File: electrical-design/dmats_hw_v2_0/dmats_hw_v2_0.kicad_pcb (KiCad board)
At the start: 2 copper layers, 2 parts, among them J1 Conn_01x05, U1 ABX00042

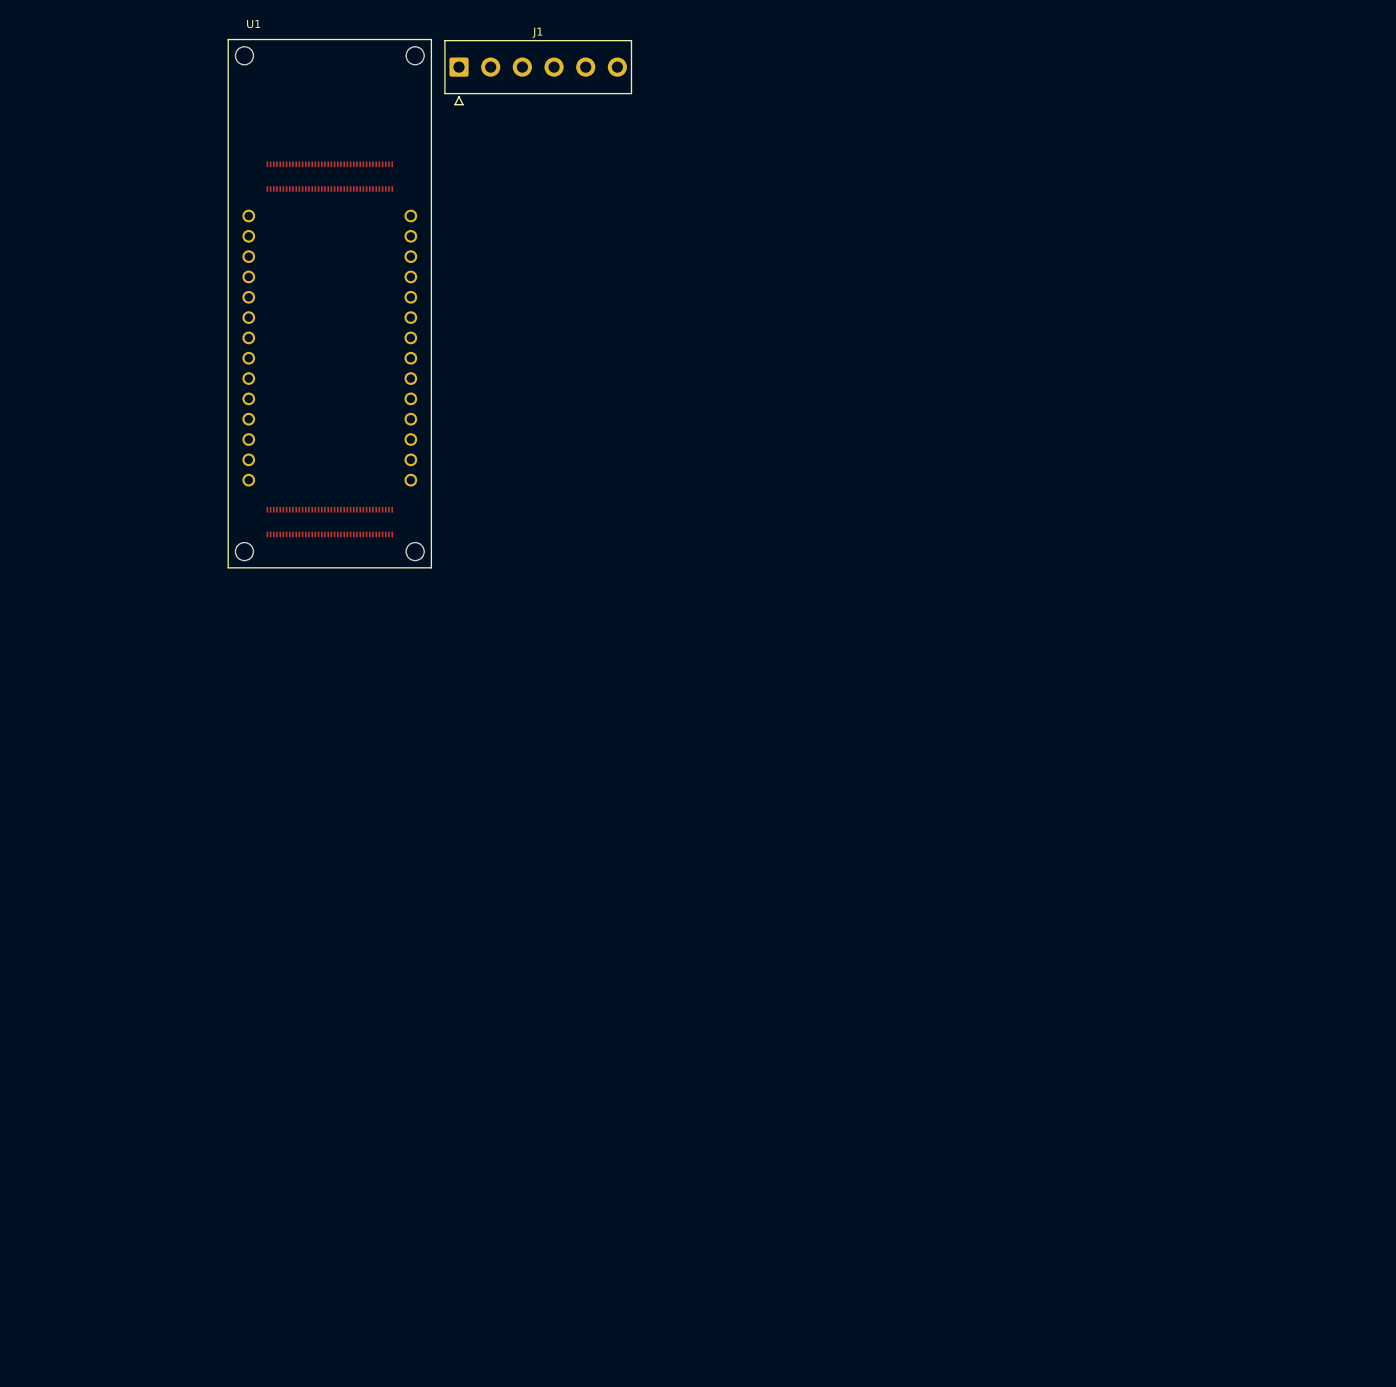
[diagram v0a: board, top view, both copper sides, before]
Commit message: bulk of PCB design layout complete
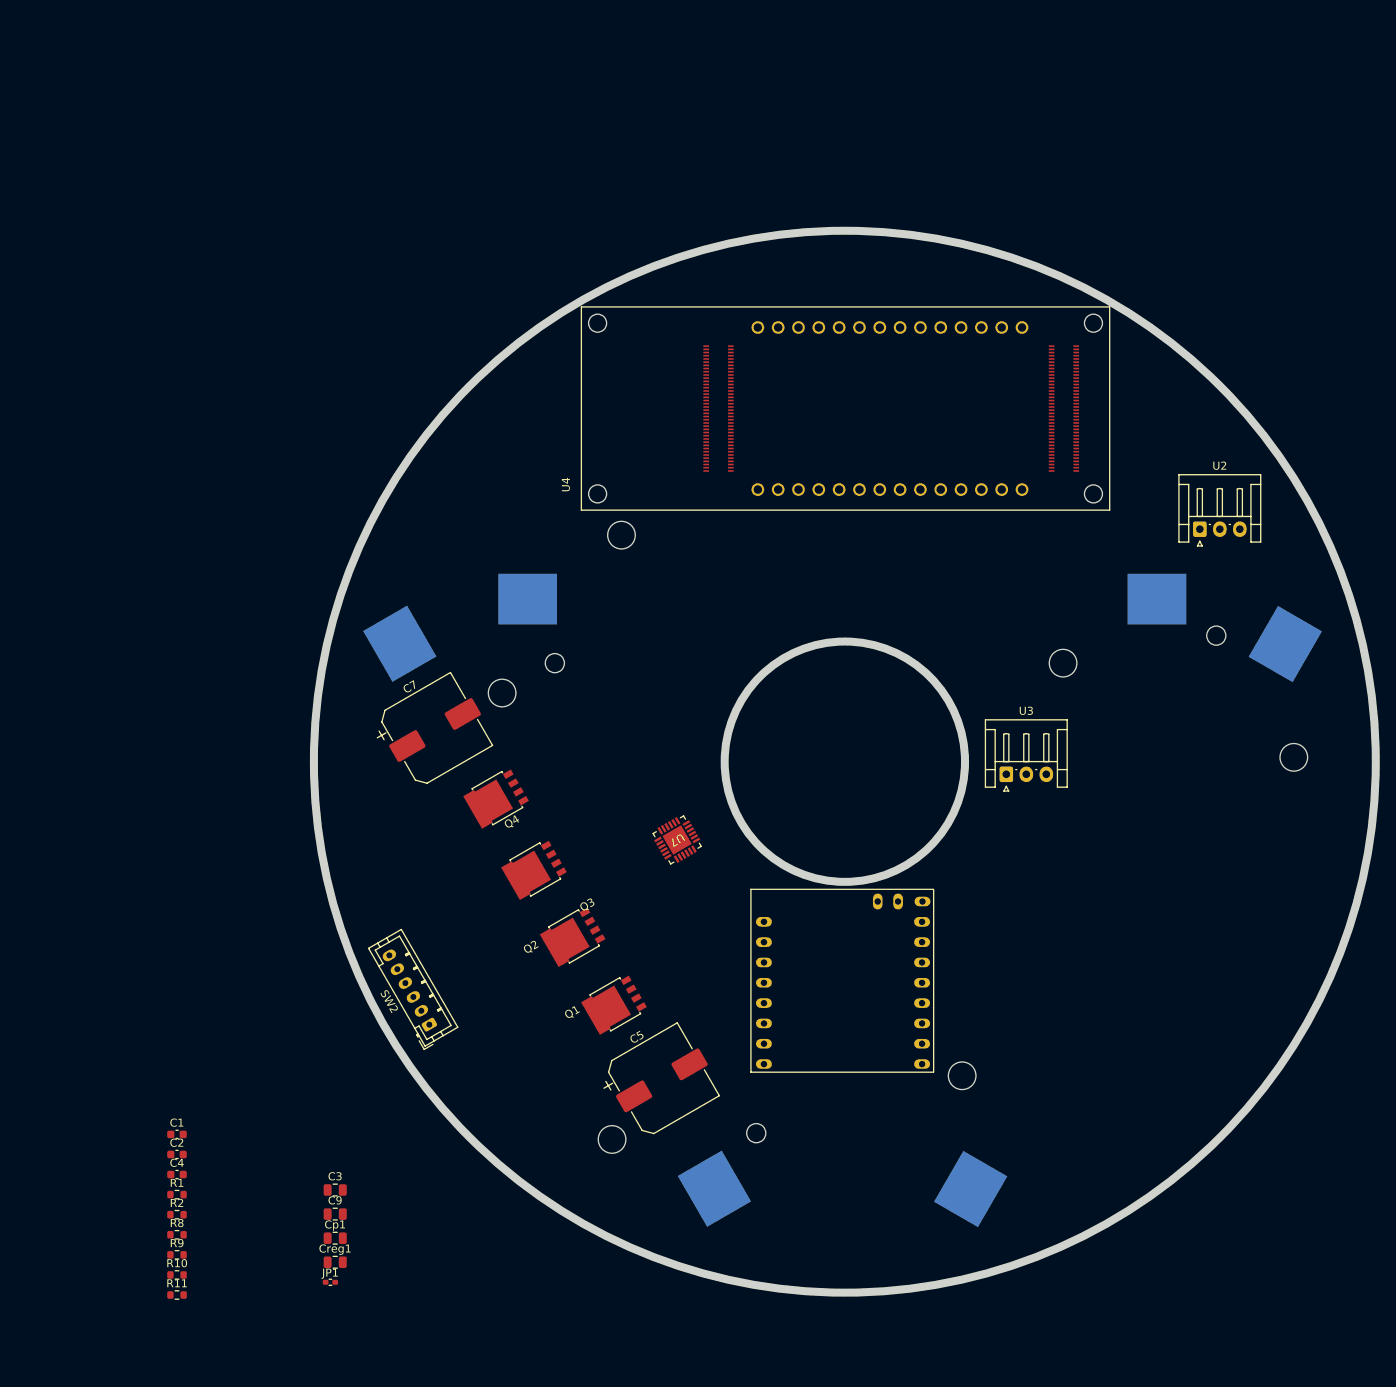
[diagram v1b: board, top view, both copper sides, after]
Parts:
- removed J1: Conn_01x05, Connector_TE-Connectivity:TE_826576-6_1x06_P3.96mm_Vertical
- added BT1: 3V7 LI-ION, Battery:BatteryHolder_Keystone_1042_1x18650, B.Cu at (195.8, 166.3)
- added BT2: 3V7 LI-ION, Battery:BatteryHolder_Keystone_1042_1x18650, B.Cu at (124.4, 166.2)
- added BT3: 3V7 LI-ION, Battery:BatteryHolder_Keystone_1042_1x18650, B.Cu at (160.1, 126.6)
- added C1: 10n, Capacitor_SMD:C_0603_1608Metric, F.Cu at (76.9, 193.5)
- added C2: 10n, Capacitor_SMD:C_0603_1608Metric, F.Cu at (76.9, 196.0)
- added C3: 10U, Capacitor_SMD:C_0805_2012Metric, F.Cu at (96.7, 200.5)
- added C4: 100N, Capacitor_SMD:C_0603_1608Metric, F.Cu at (76.9, 198.5)
- added C5: 50V 220U, Capacitor_SMD:CP_Elec_10x10, F.Cu at (137.5, 186.7)
- added C7: 50V 220U, Capacitor_SMD:CP_Elec_10x10, F.Cu at (109.2, 143.0)
- added C9: 50V 10U, Capacitor_SMD:C_0805_2012Metric, F.Cu at (96.7, 203.5)
- added Cp1: 16V 470n, Capacitor_SMD:C_0805_2012Metric, F.Cu at (96.7, 206.5)
- added Creg1: 16V 22u, Capacitor_SMD:C_0805_2012Metric, F.Cu at (96.7, 209.5)
- added JP1: Jumper_2_Open, Resistor_SMD:R_0402_1005Metric_Pad0.72x0.64mm_HandSolder, F.Cu at (96.1, 212.0)
- added Q1: PSMN1R0-30YLC,115, Package_TO_SOT_SMD:LFPAK56, F.Cu at (131.7, 177.2)
- added Q2: PSMN1R0-30YLC,115, Package_TO_SOT_SMD:LFPAK56, F.Cu at (126.5, 168.8)
- added Q3: PSMN1R0-30YLC,115, Package_TO_SOT_SMD:LFPAK56, F.Cu at (121.7, 160.4)
- added Q4: PSMN1R0-30YLC,115, Package_TO_SOT_SMD:LFPAK56, F.Cu at (117.0, 151.5)
- added R1: 10K, Resistor_SMD:R_0603_1608Metric, F.Cu at (76.9, 201.0)
- added R10: 1K, Resistor_SMD:R_0603_1608Metric, F.Cu at (76.9, 211.1)
- added R11: 1K, Resistor_SMD:R_0603_1608Metric, F.Cu at (76.9, 213.6)
- added R2: 10K, Resistor_SMD:R_0603_1608Metric, F.Cu at (76.9, 203.5)
- added R8: 1K, Resistor_SMD:R_0603_1608Metric, F.Cu at (76.9, 206.0)
- added R9: 1K, Resistor_SMD:R_0603_1608Metric, F.Cu at (76.9, 208.6)
- added SW2: Motor_2BitEncoder, Connector_JST:JST_PH_B6B-PH-K_1x06_P2.00mm_Vertical, F.Cu at (108.5, 179.8)
- added U2: A1324, Connector_JST:JST_EH_S3B-EH_1x03_P2.50mm_Horizontal, F.Cu at (204.8, 117.8)
- added U3: A1324, Connector_JST:JST_EH_S3B-EH_1x03_P2.50mm_Horizontal, F.Cu at (180.6, 148.5)
- added U4: ABX00042, DMATS_capstone:MODULE_ABX00042, F.Cu at (160.5, 102.8)
- added U7: ~, DMATS_capstone:QFN-24_ALM, F.Cu at (139.4, 156.7)
- U1: value ABX00042 -> ~; footprint ABX00042:MODULE_ABX00042 -> DMATS_capstone:ARDUINO_NICLA
- moved U1 111.2 mm to (166.3, 175.8), turned to 90 degrees
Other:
- board outline added: 132.7 x 132.7 mm

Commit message: PCB work
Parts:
- JP1: footprint Resistor_SMD:R_0402_1005Metric_Pad0.72x0.64mm_HandSolder -> Resistor_SMD:R_0603_1608Metric
- U7: footprint DMATS_capstone:QFN-24_ALM -> Package_DFN_QFN:HVQFN-24-1EP_4x4mm_P0.5mm_EP2.6x2.6mm_ThermalVias
- moved C4 80.4 mm to (143.3, 153.2), turned to 30 degrees
- moved R1 80.3 mm to (136.9, 147.6), turned to -150 degrees
- moved R2 80.1 mm to (137.3, 150.9), turned to 120 degrees
- moved JP1 75.7 mm to (139.3, 149.8), turned to 120 degrees
- moved R11 74.2 mm to (118.2, 151.9), turned to 120 degrees
- moved R10 68.2 mm to (122.3, 160.1), turned to 120 degrees
- moved Cp1 67.6 mm to (144.8, 159.0), turned to 30 degrees
- moved C2 66.9 mm to (132.1, 158.1), turned to 30 degrees
- moved C3 66.1 mm to (144.3, 154.6), turned to 30 degrees
- moved C1 65.5 mm to (134.1, 161.5), turned to 30 degrees
- moved R9 63.3 mm to (130.6, 175.2), turned to 120 degrees
- moved R8 62.6 mm to (126.6, 167.9), turned to 120 degrees
- moved Creg1 61.6 mm to (133.0, 159.7), turned to -150 degrees
- moved C9 60.8 mm to (142.0, 162.9), turned to -60 degrees
- moved Q1 11.4 mm to (121.5, 172.1)
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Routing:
- net /A4957_driver/VBB: track 0.00 -> 35.5 mm
- net /A4957_driver/GLA: track 0.00 -> 21.7 mm
- net /A4957_driver/GLB: track 0.00 -> 18.5 mm
- net /A4957_driver/GHA: track 0.00 -> 15.8 mm
- net /A4957_driver/GHB: track 0.00 -> 15.2 mm
- net +5V: track 0.00 -> 14.0 mm
- net /FAULT: track 0.00 -> 7.80 mm
- net /A4957_driver/RDEAD: track 0.00 -> 7.40 mm
- net Net-(U7-CP2): track 0.00 -> 5.65 mm
- net Net-(U7-CA): track 0.00 -> 4.44 mm
- net Net-(U7-CB): track 0.00 -> 4.39 mm
- net Net-(Q4-G): track 0.00 -> 4.10 mm
- net Net-(Q3-G): track 0.00 -> 3.92 mm
- net Net-(Q1-G): track 0.00 -> 3.78 mm
- net Net-(Q2-G): track 0.00 -> 3.55 mm
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- added copper zone on F.Cu, net /A4957_driver/VBB

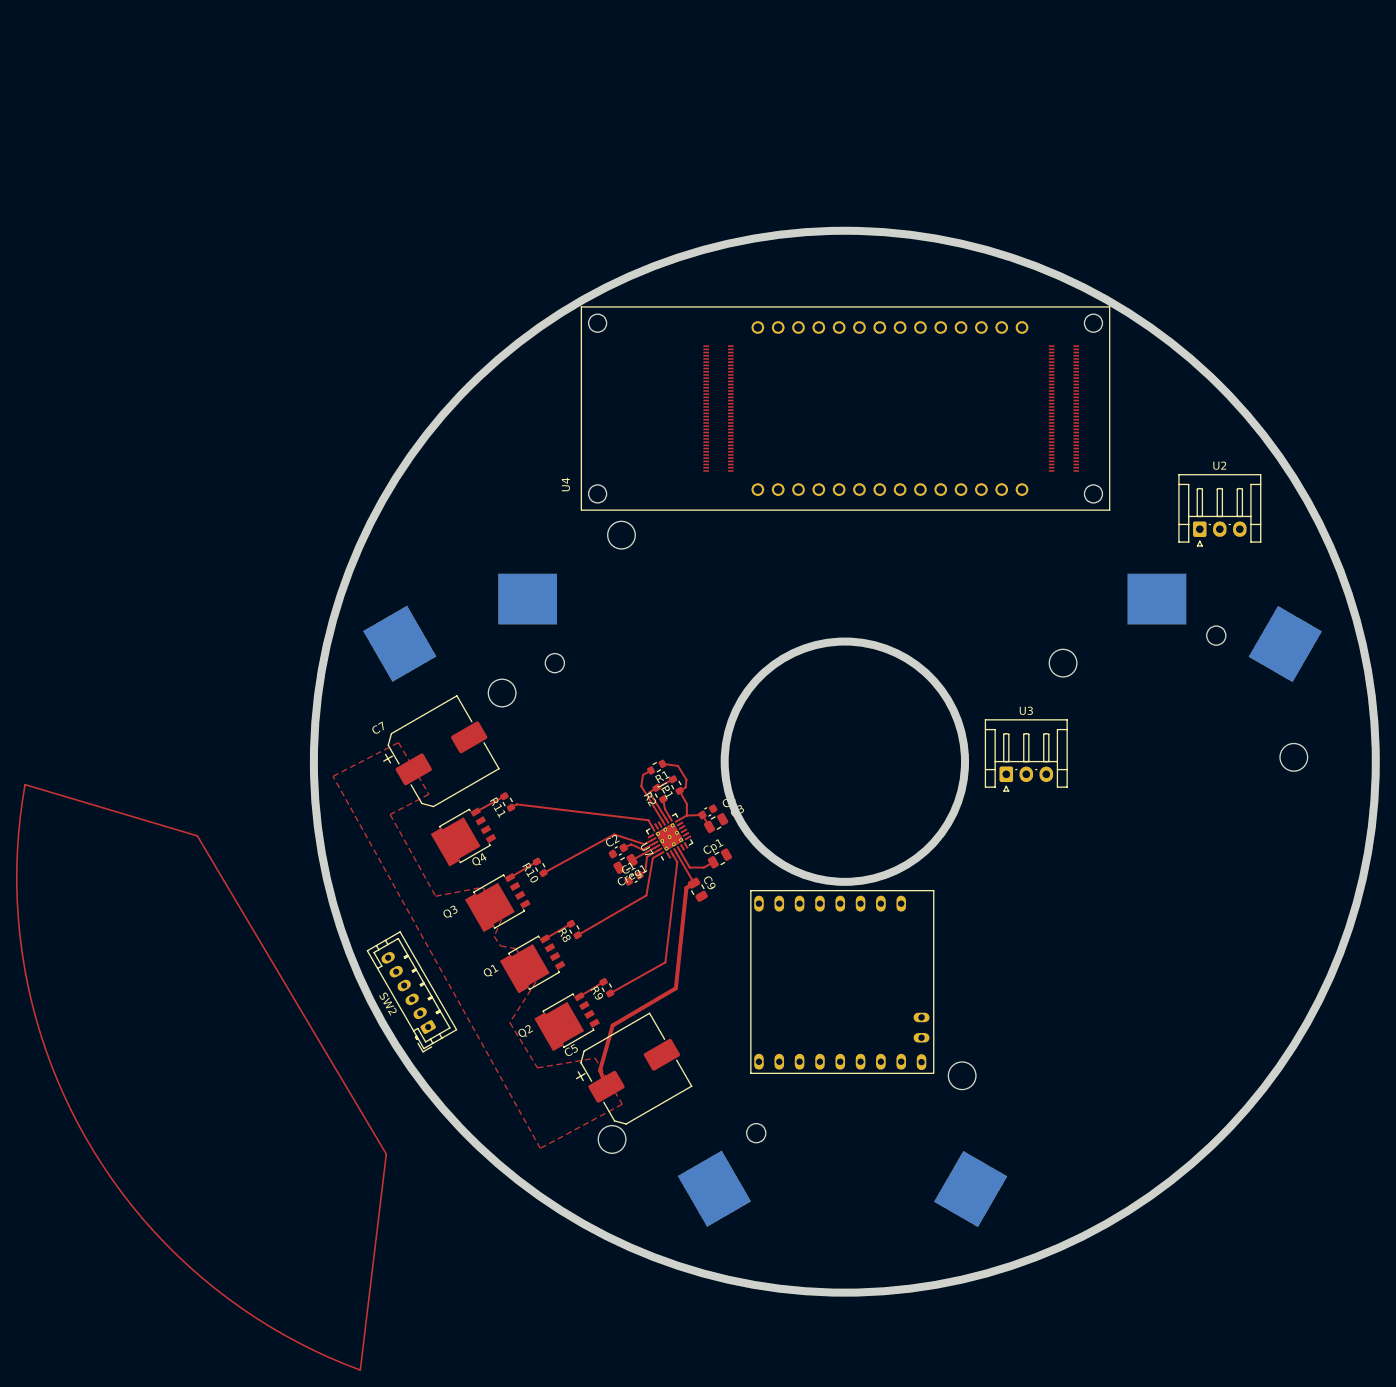
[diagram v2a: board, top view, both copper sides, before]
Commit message: completed motor driver PCB
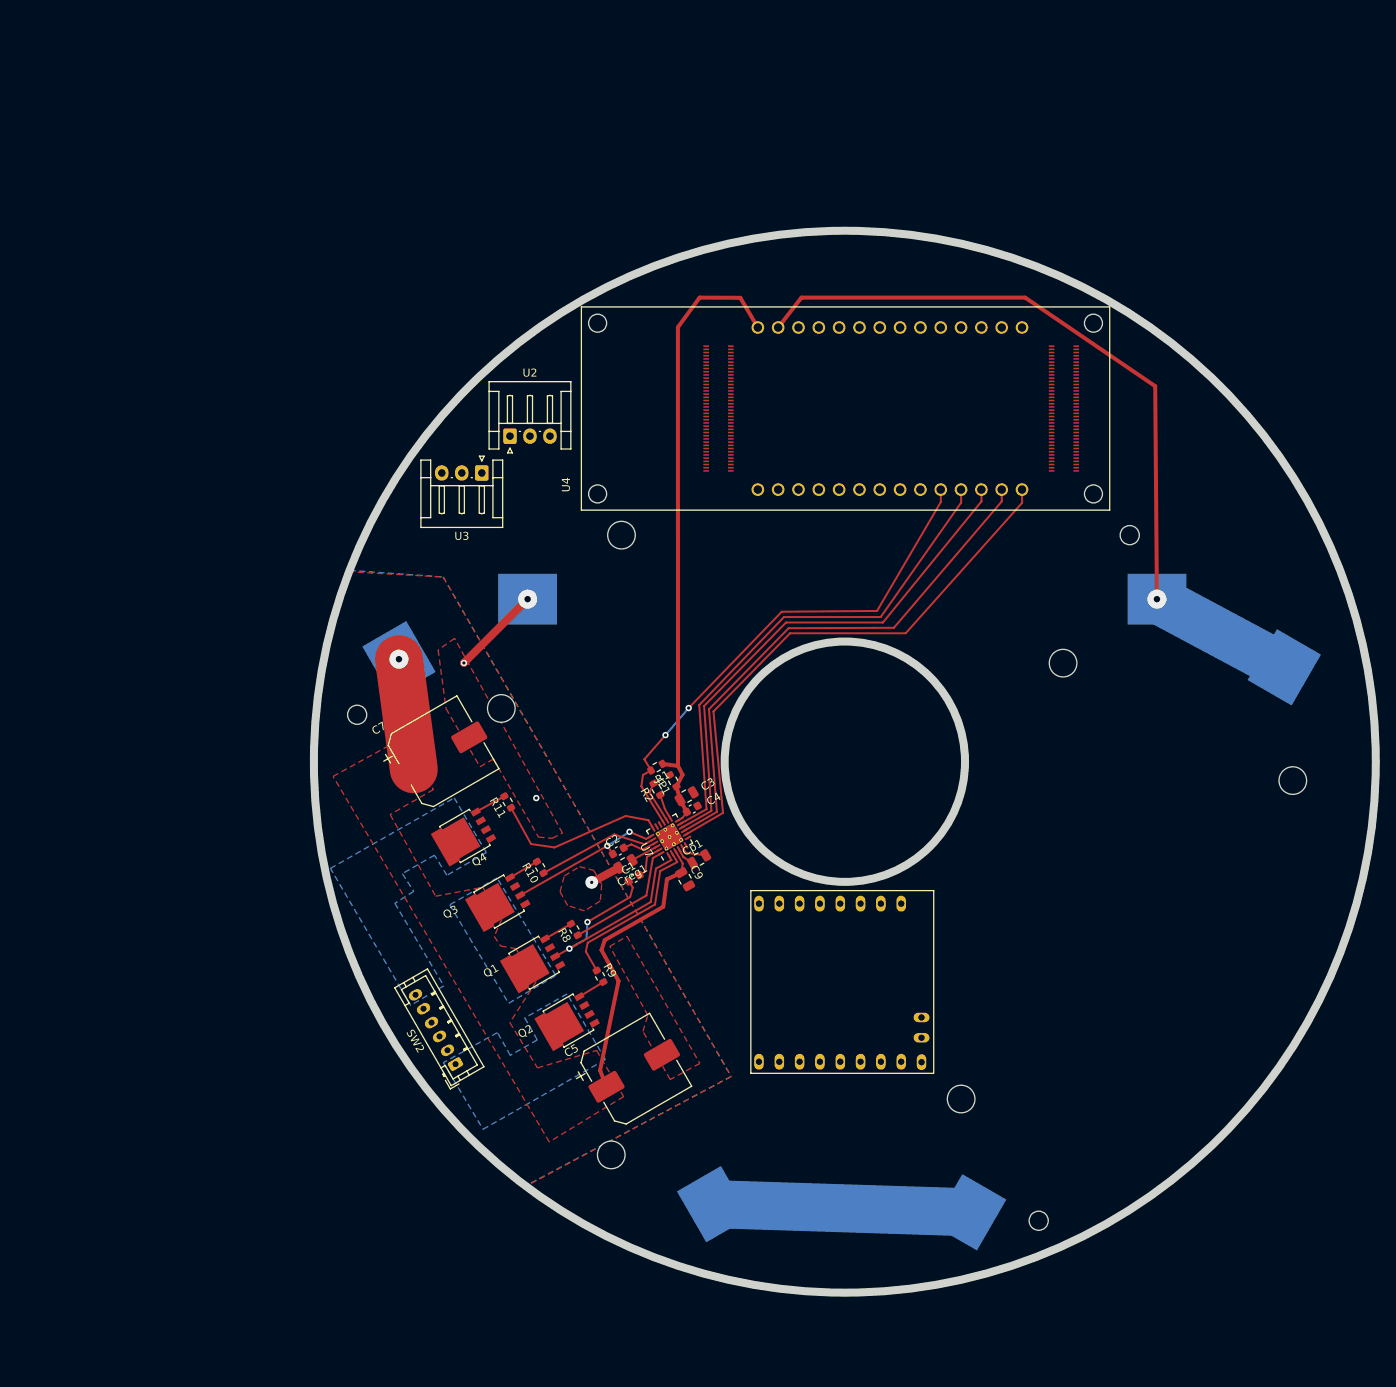
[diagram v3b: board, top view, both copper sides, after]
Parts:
- moved U2 87.0 mm to (118.5, 106.2)
- moved U3 75.6 mm to (115.0, 110.8), turned to 180 degrees
- moved SW2 5.76 mm to (111.7, 184.7)
- moved C3 4.99 mm to (140.6, 151.2)
- moved BT1 2.91 mm to (195.7, 169.2), turned to 60 degrees
- moved Cp1 2.60 mm to (142.2, 159.1)
- moved C9 2.06 mm to (140.4, 161.6)
- moved C4 1.98 mm to (141.3, 152.8)
- moved BT2 1.93 mm to (124.3, 168.2), turned to -60 degrees
- moved R9 1.66 mm to (129.8, 173.7), turned to -60 degrees
- moved JP1 0.67 mm to (138.9, 149.3)
- moved R2 0.67 mm to (136.9, 150.4)
- turned BT3 to 180 degrees
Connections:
- BT1 pad 1: +BATT -> Net-(BT1-+)
- BT1 pad 2: Net-(BT1--) -> /VIN
- BT2 pad 1: Net-(BT1--) -> +BATT
- BT2 pad 2: /VIN -> Net-(BT1-+)
- C5 pad 1: /A4957_driver/VBB -> +BATT
- C7 pad 1: /A4957_driver/VBB -> +BATT
- C9 pad 1: /A4957_driver/VBB -> +BATT
- Q1 pad 5: /A4957_driver/VBB -> +BATT
- Q3 pad 5: /A4957_driver/VBB -> +BATT
- U4 pad JA10: unconnected-(U4C-D1-PadJA10) -> /FAULT
- U4 pad JA12: /BHI -> /ALO
- U4 pad JA13: /ALO -> /BHI
- U4 pad JD14: /FAULT -> unconnected-(U4C-D6-PadJD14)
- U7 pad 3: /A4957_driver/VBB -> +BATT
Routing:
- net /VIN: track 0.00 -> 97.1 mm, vias 0 -> 1
- net /BLO: track 0.00 -> 69.7 mm
- net /BHI: track 0.00 -> 67.2 mm
- net /ALO: track 0.00 -> 65.1 mm
- net +5V: track 14.0 -> 78.7 mm
- net /AHI: track 0.00 -> 63.3 mm
- net /FAULT: track 7.80 -> 63.9 mm, vias 0 -> 2
- net +BATT: track 0.00 -> 50.0 mm, vias 0 -> 1
- net /A4957_driver/VBB: track 35.5 -> 0.00 mm
- net /M1: track 0.00 -> 33.8 mm, vias 0 -> 2
- net Net-(BT1-+): track 0.00 -> 32.0 mm
- net /M2: track 0.00 -> 20.0 mm, vias 0 -> 2
- net GND: track 2.50 -> 18.3 mm, vias 0 -> 4
- net /A4957_driver/GLB: track 18.5 -> 21.9 mm
- net Net-(U7-CP1): track 0.00 -> 3.30 mm
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- added copper zone on B.Cu, net (none)
- added copper zone on F.Cu, net +BATT
- added copper zone on B.Cu, net /M1
- added copper zone on B.Cu, net /M2
- added copper zone on B.Cu, net GND
- added copper zone on F.Cu, net GND
- removed copper zone on F.Cu, net /A4957_driver/VBB
